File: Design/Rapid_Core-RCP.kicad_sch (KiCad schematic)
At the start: 78 parts, among them IC1 TLIN1039DDFRQ1, IC2 TLIN1039DDFRQ1, IC3 SHT30A-DIS-B2.5KS, J1 CMD PIN, J2 CMD PIN, J3 LIN_1, J4 LIN_2, J5 GPIO_CONN_x_4, J6 SWD_Debug, J7 SPI, J8 USART, SW1 SW_Push, U1 STM32F446RETx, Y1 Crystal_GND24, Y2 32.768_KHz

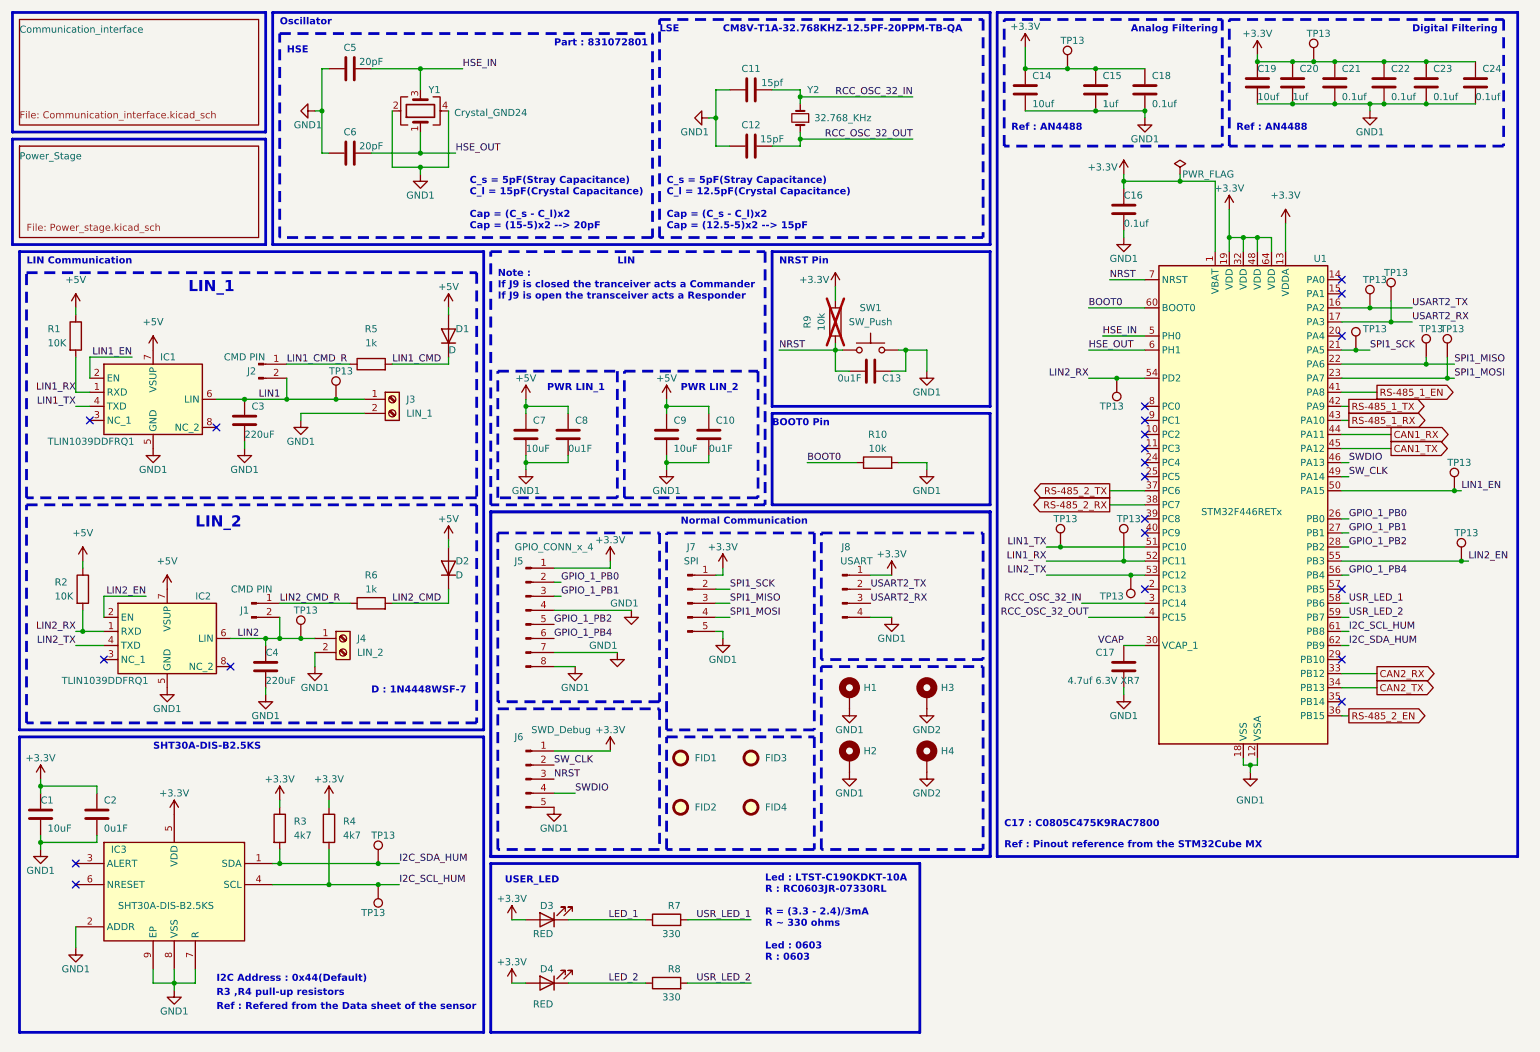
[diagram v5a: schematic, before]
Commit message: Added lib folder, Layer layed
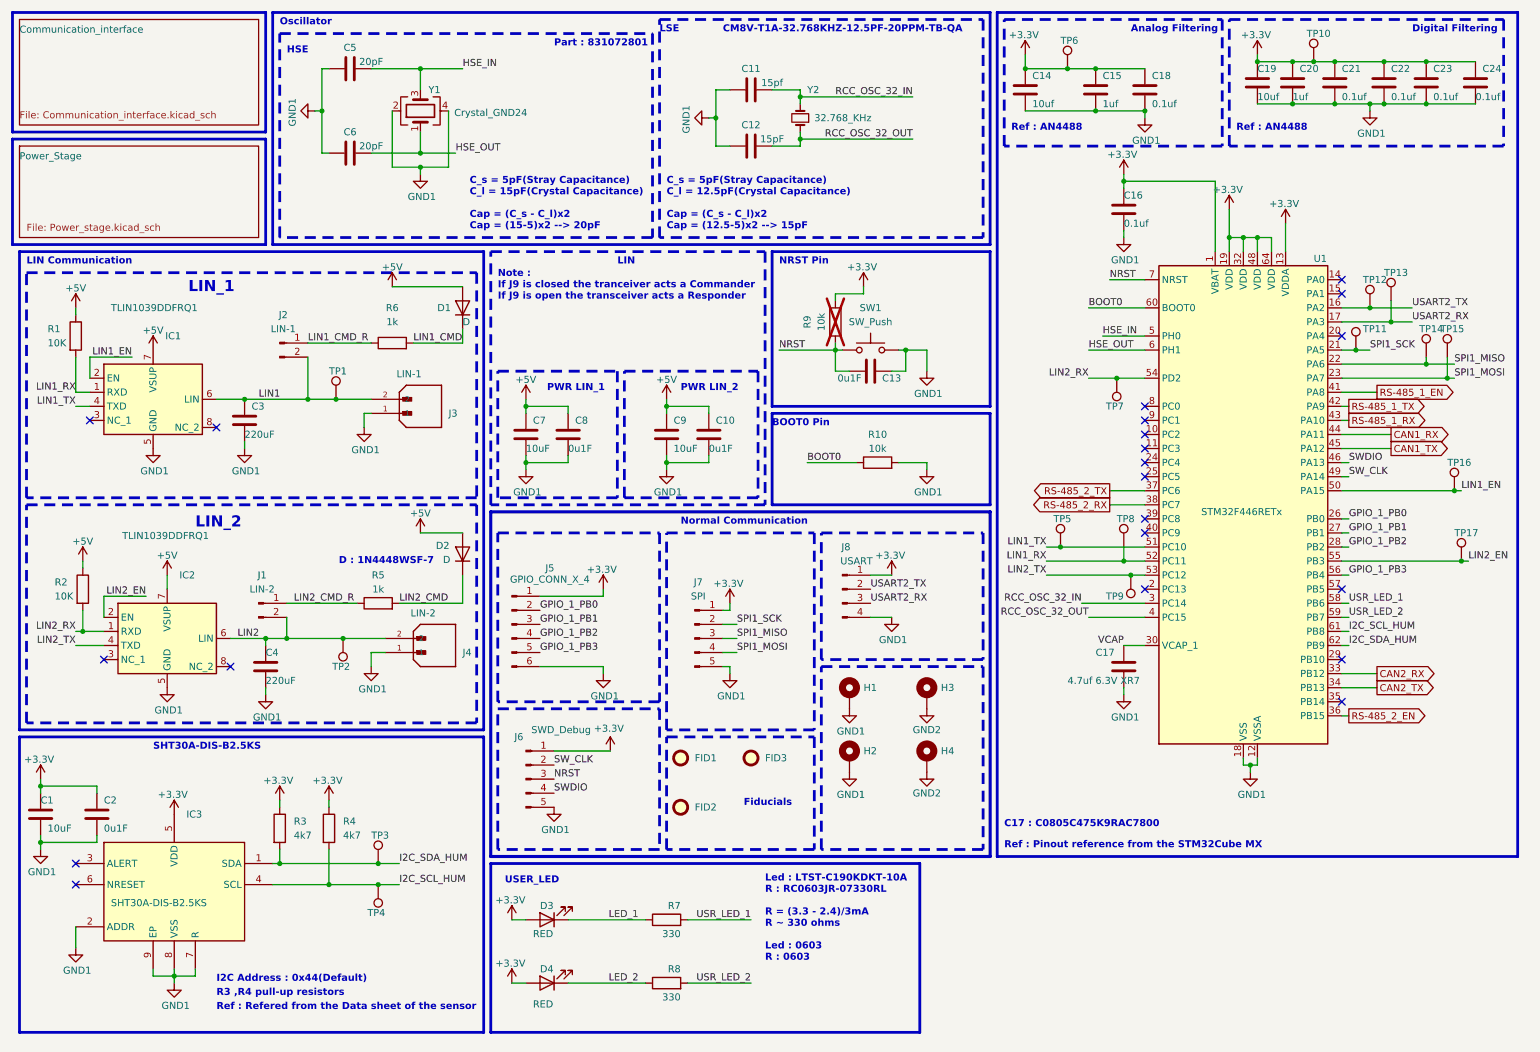
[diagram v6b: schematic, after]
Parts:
- removed FID4: Fiducial, Fiducial:Fiducial_1.5mm_Mask3mm, symbol Mechanical:Fiducial
- removed J3: LIN_1, TerminalBlock_Phoenix:TerminalBlock_Phoenix_MKDS-1,5-2_1x02_P5.00mm_Horizontal, symbol Connector:Screw_Terminal_01x02
- removed J4: LIN_2, TerminalBlock_Phoenix:TerminalBlock_Phoenix_MKDS-1,5-2_1x02_P5.00mm_Horizontal, symbol Connector:Screw_Terminal_01x02
- removed J5: GPIO_CONN_x_4, Connector_PinHeader_2.54mm:PinHeader_1x08_P2.54mm_Vertical, symbol Connector:Conn_01x08_Pin
- added J3: LIN-1, 0530480210_2pin_P1.25_PicoBlade:MOLEX_530480210, symbol 0530480210_2pin_P1.25_PicoBlade:530480210
- added J4: LIN-2, 0530480210_2pin_P1.25_PicoBlade:MOLEX_530480210, symbol 0530480210_2pin_P1.25_PicoBlade:530480210
- added J5: GPIO_CONN_X_4, Connector_PinHeader_2.54mm:PinHeader_1x06_P2.54mm_Vertical, symbol Connector:Conn_01x06_Pin
- J1: value CMD PIN -> LIN-2
- J2: value CMD PIN -> LIN-1
- renumbered R6 to R5, R5 to R6, TP13 to TP1, TP13 to TP10, TP13 to TP11, TP13 to TP12, TP13 to TP14, TP13 to TP15, TP13 to TP16, TP13 to TP17, TP13 to TP2, TP13 to TP3, TP13 to TP4, TP13 to TP5, TP13 to TP6, TP13 to TP7, TP13 to TP8, TP13 to TP9
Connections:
- net +3.3V: now also J5.1 (Pin_1)
- net GND1: now also J3.1, J4.1, J5.6 (Pin_6)
- net GPIO_1_PB0: now also J5.2 (Pin_2)
- net GPIO_1_PB1: now also J5.3 (Pin_3)
- net GPIO_1_PB2: now also J5.4 (Pin_4)
- net LIN1: now also J3.2
- net LIN2: now also J4.2
- net GPIO_1_PB4 renamed GPIO_1_PB3
- net GPIO_1_PB3: now also J5.5 (Pin_5)
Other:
- note added: "Fiducials"
- moved on the sheet: D1, D2, J7, R5, R6, TP2

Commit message: End of version 1.0.0 design
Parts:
- SW1: footprint Button_Switch_SMD:SW_SPST_CK_RS282G05A3 -> Button_Switch_SMD:SW_Tactile_SPST_NO_Straight_CK_PTS636Sx25SMTRLFS
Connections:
- net LIN1_TX is gone; now on net LIN1_RX: IC1.4 (TXD), TP5.1, U1.51 (PC10)
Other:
- moved on the sheet: C1, C10, C11, C12, C13, C14, C15, C16, C17, C18, C19, C2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

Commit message: Added everything
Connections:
- net LIN1_RX: no longer IC1.4 (TXD), TP5.1, TP8.1, U1.51 (PC10)
- new net LIN1_TX: IC1.4 (TXD), TP5.1, TP8.1, U1.51 (PC10)
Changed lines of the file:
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@@
 		(title "Rapid-Core")
 		(date "2024-09-09")
-		(rev "1.0.0")
+		(rev "1.0.1")
 	)
 	(junction
@@
 	)
 	(junction
-		(at 213.36 113.03)
-		(diameter 0)
-		(color 0 0 0 0)
-	)
-	(junction
 		(at 203.2 24.13)
 		(diameter 0)
@@
 	(wire
 		(pts
-			(xy 213.36 113.03) (xy 217.17 113.03)
+			(xy 199.39 113.03) (xy 217.17 113.03)
 		)
 		(stroke
@@
 	(wire
 		(pts
-			(xy 213.36 110.49) (xy 213.36 113.03)
-		)
-		(stroke
-			(width 0)
-			(type default)
-		)
-	)
-	(wire
-		(pts
 			(xy 260.35 22.86) (xy 267.97 22.86)
 		)
@@
 	(wire
 		(pts
-			(xy 199.39 113.03) (xy 213.36 113.03)
-		)
-		(stroke
-			(width 0)
-			(type default)
-		)
-	)
-	(wire
-		(pts
 			(xy 207.01 123.19) (xy 217.17 123.19)
 		)
@@
 	)
 	(symbol
-		(lib_name "STM32F446RETx_1")
-		(lib_id "MCU_ST_STM32F4:STM32F446RETx")
-		(at 234.95 102.87 0)
-		(unit 1)
-		(exclude_from_sim no)
-		(in_bom yes)
-		(on_board yes)
-		(dnp no)
-		(property "Reference" "U1"
-			(at 247.65 58.42 0)
-			(effects
-				(font
-					(size 1.27 1.27)
-				)
-				(justify left)
-			)
-		)
-		(property "Value" "STM32F446RETx"
-			(at 227.33 104.14 0)
-			(effects
-				(font
-					(size 1.27 1.27)
-				)
-				(justify left)
-			)
-		)
-		(property "Footprint" "Package_QFP:LQFP-64_10x10mm_P0.5mm"
-			(at 219.71 146.05 0)
-			(effects
-				(font
-					(size 1.27 1.27)
-				)
-				(justify right)
-				(hide yes)
-			)
-		)
-		(property "Datasheet" "https://www.st.com/resource/en/datasheet/stm32f446re.pdf"
-			(at 234.95 102.87 0)
-			(effects
-				(font
-					(size 1.27 1.27)
-				)
-				(hide yes)
-			)
-		)
-		(property "Description" ""
-			(at 234.95 102.87 0)
-			(effects
-				(font
-					(size 1.27 1.27)
-				)
-				(hide yes)
-			)
-		)
-		(pin "1"
-		)
-		(pin "10"
-		)
-		(pin "11"
-		)
-		(pin "12"
-		)
-		(pin "13"
-		)
-		(pin "14"
-		)
-		(pin "15"
-		)
-		(pin "16"
-		)
-		(pin "17"
-		)
-		(pin "18"
-		)
-		(pin "19"
-		)
-		(pin "2"
-		)
-		(pin "20"
-		)
-		(pin "21"
-		)
-		(pin "22"
-		)
-		(pin "23"
-		)
-		(pin "24"
-		)
-		(pin "25"
-		)
-		(pin "26"
-		)
-		(pin "27"
-		)
-		(pin "28"
-		)
-		(pin "29"
-		)
-		(pin "3"
-		)
-		(pin "30"
-		)
-		(pin "31"
-		)
-		(pin "32"
-		)
-		(pin "33"
-		)
-		(pin "34"
-		)
-		(pin "35"
-		)
-		(pin "36"
-		)
-		(pin "37"
-		)
-		(pin "38"
-		)
-		(pin "39"
-		)
-		(pin "4"
-		)
-		(pin "40"
-		)
-		(pin "41"
-		)
-		(pin "42"
-		)
-		(pin "43"
-		)
-		(pin "44"
-		)
-		(pin "45"
-		)
-		(pin "46"
-		)
-		(pin "47"
-		)
-		(pin "48"
-		)
-		(pin "49"
-		)
-		(pin "5"
-		)
-		(pin "50"
-		)
-		(pin "51"
-		)
-		(pin "52"
-		)
-		(pin "53"
-		)
-		(pin "54"
-		)
-		(pin "55"
-		)
-		(pin "56"
-		)
-		(pin "57"
-		)
-		(pin "58"
-		)
-		(pin "59"
-		)
-		(pin "6"
-		)
-		(pin "60"
-		)
-		(pin "61"
-		)
-		(pin "62"
-		)
-		(pin "63"
-		)
-		(pin "64"
-		)
-		(pin "7"
-		)
-		(pin "8"
-		)
-		(pin "9"
-		)
-		(instances
-			(project "Rapid_Core-RCP"
-				(path "/1a5d67a4-b410-4c7a-b64e-9e0193c8e6b4"
-					(reference "U1")
-					(unit 1)
-				)
-			)
-		)
-	)
-	(symbol
 		(lib_name "+5V_1")
 		(lib_id "power:+5V")
@@
 					(unit 1)
 				)
+			)
+		)
+	)
+	(symbol
+		(lib_id "MCU_ST_STM32F4:STM32F446RETx")
+		(at 234.95 102.87 0)
+		(unit 1)
+		(exclude_from_sim no)
+		(in_bom yes)
+		(on_board yes)
+		(dnp no)
+		(fields_autoplaced yes)
+		(property "Reference" "U1"
+			(at 239.6841 148.59 0)
+			(effects
+				(font
+					(size 1.27 1.27)
+				)
+				(justify left)
+			)
+		)
+		(property "Value" "STM32F446RETx"
+			(at 239.6841 151.13 0)
+			(effects
+				(font
+					(size 1.27 1.27)
+				)
+				(justify left)
+			)
+		)
+		(property "Footprint" "Package_QFP:LQFP-64_10x10mm_P0.5mm"
+			(at 219.71 146.05 0)
+			(effects
+				(font
+					(size 1.27 1.27)
+				)
+				(justify right)
+				(hide yes)
+			)
+		)
+		(property "Datasheet" "https://www.st.com/resource/en/datasheet/stm32f446re.pdf"
+			(at 234.95 102.87 0)
+			(effects
+				(font
+					(size 1.27 1.27)
+				)
+				(hide yes)
+			)
+		)
+		(property "Description" "STMicroelectronics Arm Cortex-M4 MCU, 512KB flash, 128KB RAM, 180 MHz, 1.8-3.6V, 50 GPIO, LQFP64"
+			(at 234.95 102.87 0)
+			(effects
+				(font
+					(size 1.27 1.27)
+				)
+				(hide yes)
+			)
+		)
+		(pin "4"
+		)
+		(pin "25"
+		)
+		(pin "40"
+		)
+		(pin "38"
+		)
+		(pin "42"
+		)
+		(pin "50"
+		)
+		(pin "51"
+		)
+		(pin "14"
+		)
+		(pin "17"
+		)
+		(pin "24"
+		)
+		(pin "45"
+		)
+		(pin "52"
+		)
+		(pin "28"
+		)
+		(pin "54"
+		)
+		(pin "48"
+		)
+		(pin "56"
+		)
+		(pin "59"
+		)
+		(pin "6"
+		)
+		(pin "1"
+		)
+		(pin "31"
+		)
+		(pin "13"
+		)
+		(pin "27"
+		)
+		(pin "43"
+		)
+		(pin "60"
+		)
+		(pin "20"
+		)
+		(pin "23"
+		)
+		(pin "29"
+		)
+		(pin "34"
+		)
+		(pin "10"
+		)
+		(pin "18"
+		)
+		(pin "44"
+		)
+		(pin "21"
+		)
+		(pin "11"
+		)
+		(pin "2"
+		)
+		(pin "49"
+		)
+		(pin "33"
+		)
+		(pin "5"
+		)
+		(pin "39"
+		)
+		(pin "61"
+		)
+		(pin "55"
+		)
+		(pin "62"
+		)
+		(pin "64"
+		)
+		(pin "30"
+		)
+		(pin "7"
+		)
+		(pin "19"
+		)
+		(pin "37"
+		)
+		(pin "57"
+		)
+		(pin "32"
+		)
+		(pin "47"
+		)
+		(pin "15"
+		)
+		(pin "26"
+		)
+		(pin "63"
+		)
+		(pin "41"
+		)
+		(pin "8"
+		)
+		(pin "9"
+		)
+		(pin "46"
+		)
+		(pin "53"
+		)
+		(pin "58"
+		)
+		(pin "12"
+		)
+		(pin "16"
+		)
+		(pin "3"
+		)
+		(pin "22"
+		)
+		(pin "35"
+		)
+		(pin "36"
+		)
+		(instances
+			(project ""
+				(path "/1a5d67a4-b410-4c7a-b64e-9e0193c8e6b4"
+					(reference "U1")
+					(unit 1)
+				)
